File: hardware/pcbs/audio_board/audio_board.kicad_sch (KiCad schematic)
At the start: 26 parts, among them J2 I2C, J3 AudioJack3, J9 SPI, U4 MCP1700x-330xxMB, U5 AP7313-18SAG-7

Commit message: audio_board, power_board: update shop and part links
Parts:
- C5, C6: Part (none) -> C 10uF 16V 0805
- J2: Part (none) -> Header_1x04
- J3: Part (none) -> SJ1-3533NG; Shop (none) -> https://eu.mouser.com/ProductDetail/490-SJ1-3533NG
- J9: Part (none) -> Header_1x06
- R11, R12, R13, R14: Part (none) -> R 1kΩ 0603
- U4: Part (none) -> MCP1700T-3302E/MB; Shop (none) -> https://store.comet.bg/Catalogue/Product/6561/
- U4: Part (none) -> 2x Header_1x24
- U5: Part (none) -> AP7313-18SAG-7; Shop (none) -> https://eu.mouser.com/ProductDetail/Diodes-Incorporated/AP7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
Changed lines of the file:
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@@
 			)
 		)
+		(property "Part" "R 1kΩ 0603"
+			(at 34.29 25.4 0)
+			(effects
+				(font
+					(size 1.27 1.27)
+				)
+				(hide yes)
+			)
+		)
 		(pin "1"
 		)
@@
 			)
 		)
+		(property "Part" "C 10uF 16V 0805"
+			(at 52.07 180.34 0)
+			(effects
+				(font
+					(size 1.27 1.27)
+				)
+				(hide yes)
+			)
+		)
 		(pin "1"
 		)
@@
 			)
 		)
+		(property "Part" "R 1kΩ 0603"
+			(at 26.67 25.4 0)
+			(effects
+				(font
+					(size 1.27 1.27)
+				)
+				(hide yes)
+			)
+		)
 		(pin "1"
 		)
@@
 			)
 		)
+		(property "Part" "C 10uF 16V 0805"
+			(at 69.85 180.34 0)
+			(effects
+				(font
+					(size 1.27 1.27)
+				)
+				(hide yes)
+			)
+		)
 		(pin "1"
 		)
@@
 			)
 		)
+		(property "Part" "R 1kΩ 0603"
+			(at 48.26 25.4 0)
+			(effects
+				(font
+					(size 1.27 1.27)
+				)
+				(hide yes)
+			)
+		)
 		(pin "1"
 		)
@@
 			)
 		)
+		(property "Part" " SJ1-3533NG "
+			(at 132.08 116.84 0)
+			(effects
+				(font
+					(size 1.27 1.27)
+				)
+				(hide yes)
+			)
+		)
+		(property "Shop" "https://eu.mouser.com/ProductDetail/490-SJ1-3533NG"
+			(at 132.08 116.84 0)
+			(effects
+				(font
+					(size 1.27 1.27)
+				)
+				(hide yes)
+			)
+		)
 		(pin "R"
 		)
@@
 			)
 		)
+		(property "Part" "MCP1700T-3302E/MB"
+			(at 39.37 175.26 0)
+			(effects
+				(font
+					(size 1.27 1.27)
+				)
+				(hide yes)
+			)
+		)
+		(property "Shop" "https://store.comet.bg/Catalogue/Product/6561/"
+			(at 39.37 175.26 0)
+			(effects
+				(font
+					(size 1.27 1.27)
+				)
+				(hide yes)
+			)
+		)
 		(pin "1"
 		)
@@
 			)
 		)
+		(property "Part" "Header_1x04"
+			(at 73.66 133.35 0)
+			(effects
+				(font
+					(size 1.27 1.27)
+				)
+				(hide yes)
+			)
+		)
 		(pin "1"
 		)
@@
 			)
 		)
+		(property "Part" "R 1kΩ 0603"
+			(at 40.64 25.4 0)
+			(effects
+				(font
+					(size 1.27 1.27)
+				)
+				(hide yes)
+			)
+		)
 		(pin "1"
 		)
@@
 			)
 		)
+		(property "Part" "C 10uF 16V 0805"
+			(at 95.25 180.34 0)
+			(effects
+				(font
+					(size 1.27 1.27)
+				)
+				(hide yes)
+			)
+		)
 		(pin "1"
 		)
@@
 			)
 		)
+		(property "Part" "C 10uF 16V 0805"
+			(at 118.11 180.34 0)
+			(effects
+				(font
+					(size 1.27 1.27)
+				)
+				(hide yes)
+			)
+		)
 		(pin "1"
 		)
@@
 			)
 		)
+		(property "Part" "AP7313-18SAG-7 "
+			(at 130.81 171.45 0)
+			(effects
+				(font
+					(size 1.27 1.27)
+				)
+				(hide yes)
+			)
+		)
+		(property "Shop" "https://eu.mouser.com/ProductDetail/Diodes-Incorporated/AP7313-18SAG-7?qs=vIZ3oKQCLxpD8%252Bvczs1wyQ%3D%3D"
+			(at 130.81 171.45 0)
+			(effects
+				(font
+					(size 1.27 1.27)
+				)
+				(hide yes)
+			)
+		)
 		(pin "1"
 		)
@@
 			)
 		)
+		(property "Part" "2x Header_1x24"
+			(at 38.1 48.26 0)
+			(effects
+				(font
+					(size 1.27 1.27)
+				)
+				(hide yes)
+			)
+		)
 		(pin "0"
 		)
@@
 			)
 		)
+		(property "Part" "C 10uF 16V 0805"
+			(at 26.67 180.34 0)
+			(effects
+				(font
+					(size 1.27 1.27)
+				)
+				(hide yes)
+			)
+		)
 		(pin "1"
 		)
@@
 			)
 		)
+		(property "Part" "Header_1x06"
+			(at 81.28 107.95 0)
+			(effects
+				(font
+					(size 1.27 1.27)
+				)
+				(hide yes)
+			)
+		)
 		(pin "1"
 		)
@@
 			)
 		)
+		(property "Part" "C 10uF 16V 0805"
+			(at 146.05 180.34 0)
+			(effects
+				(font
+					(size 1.27 1.27)
+				)
+				(hide yes)
+			)
+		)
 		(pin "1"
 		)
@@
 			(at 82.55 175.26 0)
 			(effects
+				(font
+					(size 1.27 1.27)
+				)
+				(hide yes)
+			)
+		)
+		(property "Part" "MCP1700T-3302E/MB"
+			(at 82.55 175.26 0)
+			(effects
+				(font
+					(size 1.27 1.27)
+				)
+				(hide yes)
+			)
+		)
+		(property "Shop" "https://store.comet.bg/Catalogue/Product/6561/"
+			(at 82.55 175.26 0)
+			(effects

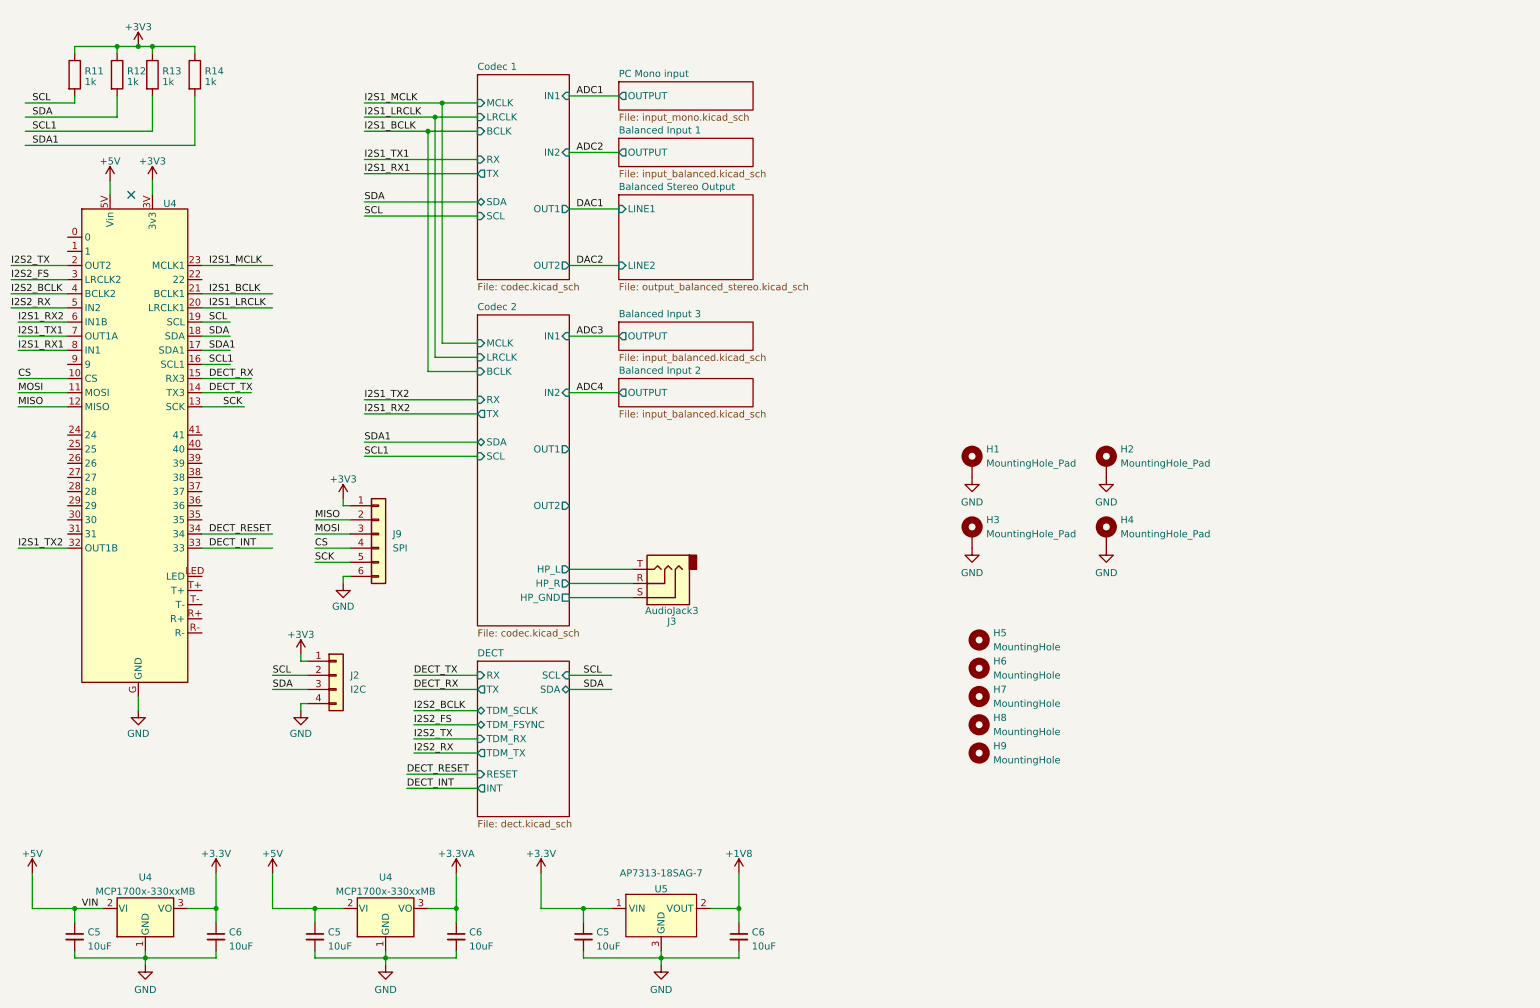
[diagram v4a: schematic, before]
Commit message: Audio board revision C
* Switched the neutrik jacks to NC3FAH2 instead of FAH1 so the jacks
  with an extra ground pin fit (but the FAH1 ones also still fit)
* Added traces for optional leds (marked DNP)
* Fixed up the opamp orientation for the XLR outputs
* Moved the LCD connector to the other side of the board and switched to
  an MTA-100 connector
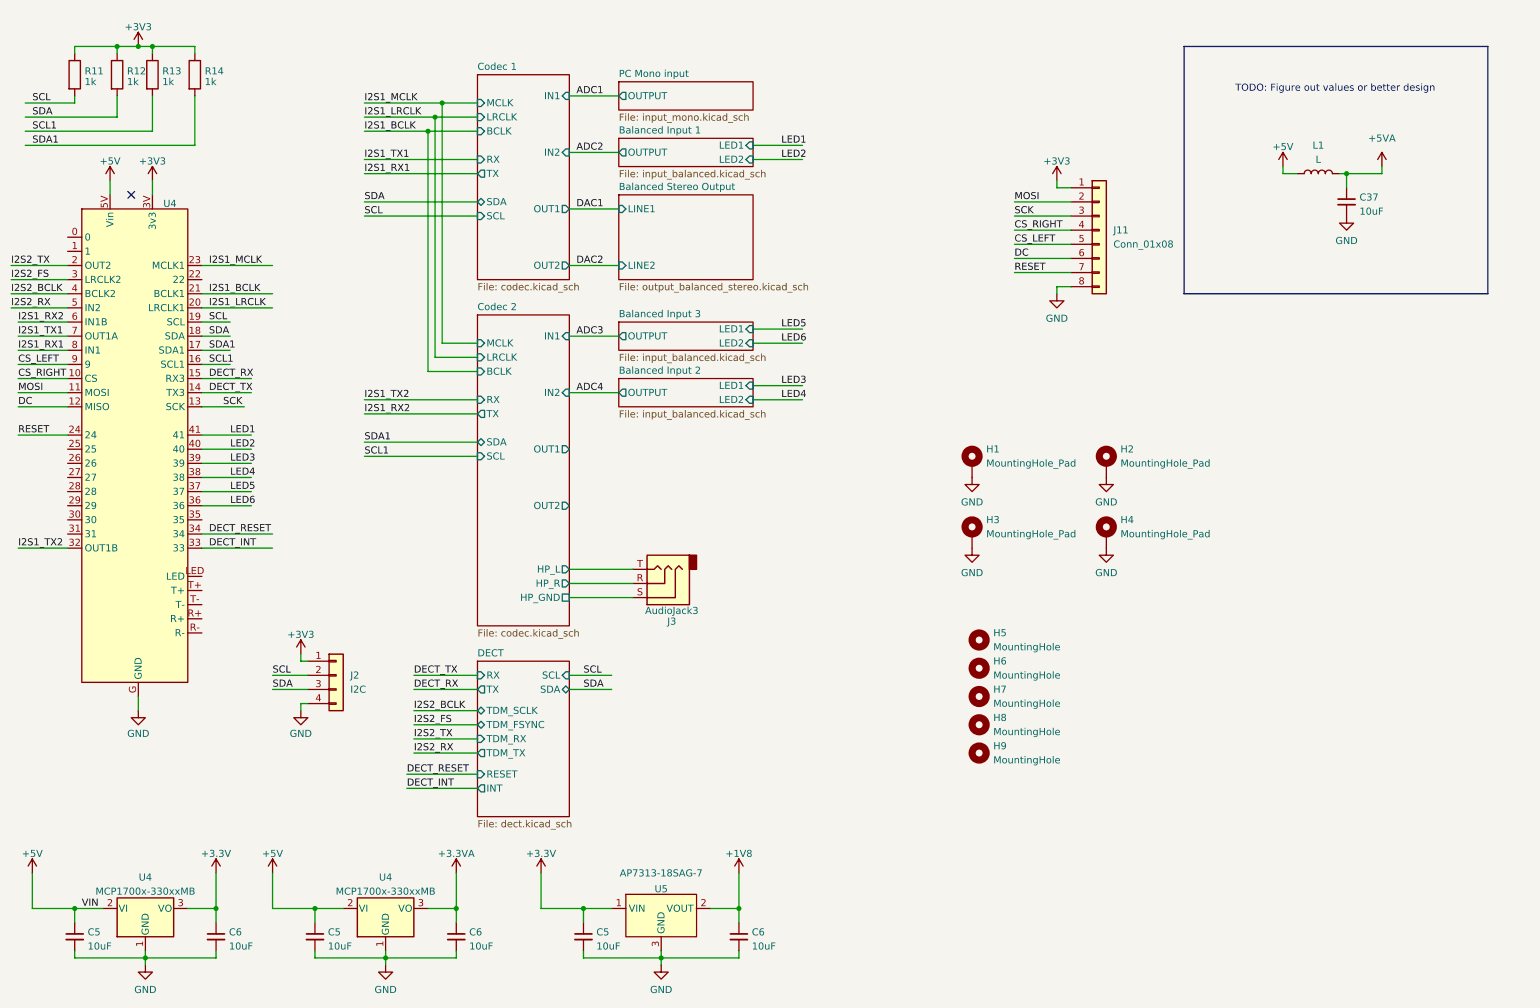
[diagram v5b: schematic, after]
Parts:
- removed J9: SPI, Connector_PinHeader_2.54mm:PinHeader_1x06_P2.54mm_Vertical, symbol Connector_Generic:Conn_01x06
- added C37: 10uF, Capacitor_SMD:C_0805_2012Metric_Pad1.18x1.45mm_HandSolder, symbol Device:C_Small
- added J11: Conn_01x08, Library:mta100_01x8_P2.54_647050-8, symbol Connector_Generic:Conn_01x08
- added L1: L, Inductor_SMD:L_0805_2012Metric, symbol Device:L
- C5, C6: Part C 10uF 16V 0805 -> (none)
- J2: Part Header_1x04 -> (none)
- J3: Part SJ1-3533NG -> (none); Shop https://eu.mouser.com/ProductDetail/490-SJ1-3533NG -> (none)
- R11, R12, R13, R14: Part R 1kΩ 0603 -> (none)
- U4: Part MCP1700T-3302E/MB -> (none); Shop https://store.comet.bg/Catalogue/Product/6561/ -> (none)
- U4: Part 2x Header_1x24 -> (none)
- U5: Part AP7313-18SAG-7 -> (none); Shop https://eu.mouser.com/ProductDetail/Diodes-Incorporated/AP7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 -> (none)
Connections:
- net +3V3: now also J11.1 (Pin_1)
- net +5V: now also L1.1
- net GND: now also C37.2, J11.8 (Pin_8)
- net MOSI: now also J11.2 (Pin_2)
- net SCK: now also J11.3 (Pin_3)
- net RESET: now reaches U4.24
- net RESET: now also J11.7 (Pin_7)
- net LED6: now reaches U4.36
- net LED5: now reaches U4.37
- net LED4: now reaches U4.38
- net LED3: now reaches U4.39
- net LED2: now reaches U4.40
- net LED1: now reaches U4.41
- net CS_LEFT: now reaches U4.9
- net CS_LEFT: now also J11.5 (Pin_5)
- net CS renamed CS_RIGHT
- net CS_RIGHT: now also J11.4 (Pin_4)
- net MISO renamed DC
- net DC: now also J11.6 (Pin_6)
- new net +5VA: C37.1, L1.2
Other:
- sheet Balanced Input 1 ports: added LED1, LED2; removed none
- sheet Balanced Input 2 ports: added LED1, LED2; removed none
- sheet Balanced Input 3 ports: added LED1, LED2; removed none
- note added: "TODO: Figure out values or better design"

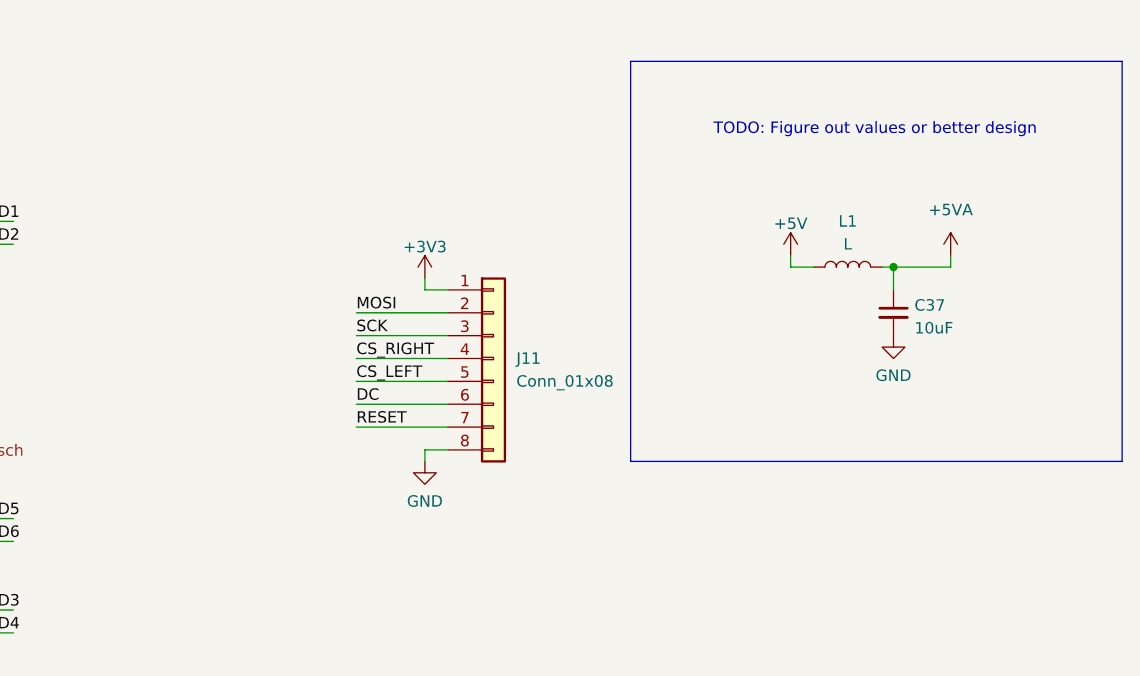
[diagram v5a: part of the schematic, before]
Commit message: Audio board Rev. C fixes
* Switch opamp to OPA1678
* Fix filter resistor on inputs from 22 ohm to 220 ohm
* Make the board 4 layers for a better ground plane
* Implement an RC filter for the opamp 5V line
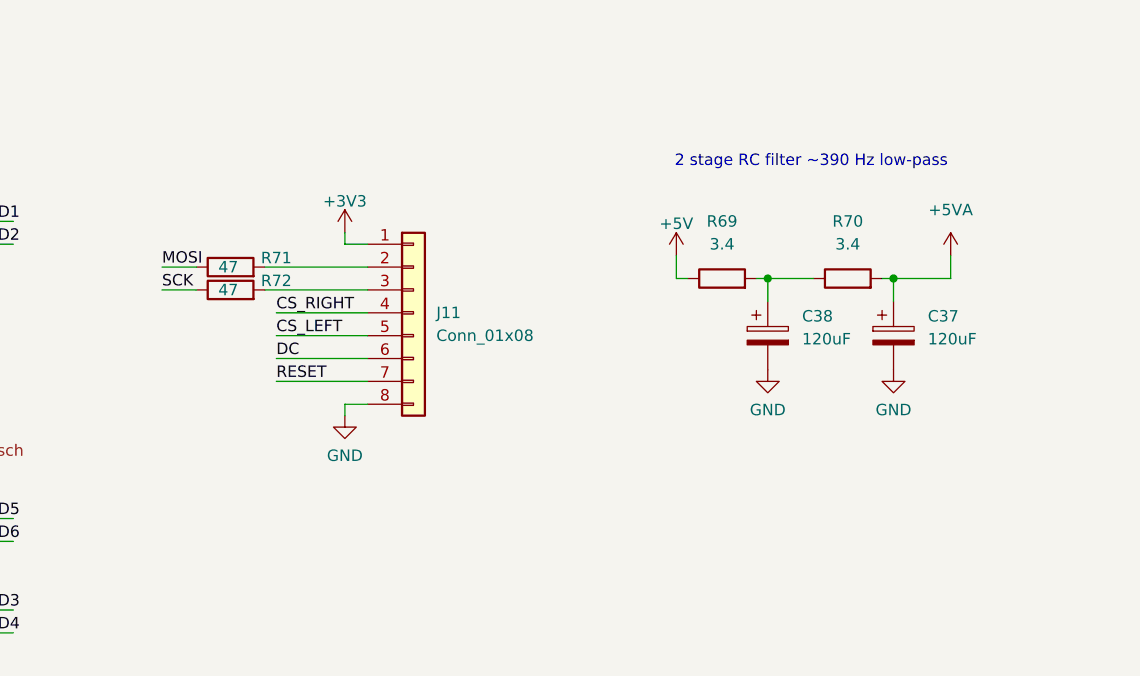
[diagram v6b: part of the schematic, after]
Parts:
- removed C37: 10uF, Capacitor_SMD:C_0805_2012Metric_Pad1.18x1.45mm_HandSolder, symbol Device:C_Small
- removed L1: L, Inductor_SMD:L_0805_2012Metric, symbol Device:L
- added C37, C38: 120uF, Capacitor_THT:CP_Radial_D5.0mm_P2.00mm, symbol Device:C_Polarized
- added R69, R70: 3.4, Resistor_SMD:R_0603_1608Metric_Pad0.98x0.95mm_HandSolder, symbol Device:R
- added R71, R72: 47, Resistor_SMD:R_0603_1608Metric, symbol Device:R
- C5, C6: MPN (none) -> 885012107014
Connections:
- net +5V: now also R69.1
- net +5VA: now also C37.1, R70.2
- net GND: now also C37.2, C38.2
- net MOSI: now also R71.1; no longer J11.2 (Pin_2)
- net SCK: now also R72.1; no longer J11.3 (Pin_3)
- new net: J11.2 (Pin_2), R71.2
- new net: J11.3 (Pin_3), R72.2
- new net: C38.1, R69.2, R70.1
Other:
- note added: "2 stage RC filter ~390 Hz low-pass"
- note removed: "TODO: Figure out values or better design"
- moved on the sheet: J11

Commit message: pcbs: update purchase info
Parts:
- C37, C38: Part (none) -> CP 120μF 16V P2; Shop (none) -> https://store.comet.bg/Catalogue/Product/29518/
- C5, C6: Part (none) -> C 10μF 16V 0805; Shop (none) -> https://store.comet.bg/Catalogue/Product/36934/
- J11: MPN (none) -> 640456-8; Part (none) -> 640456-8; Shop (none) -> https://eu.mouser.com/ProductDetail/TE-Connectivity-AMP/640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
- J2: Part (none) -> Header_1x04
- J3: Part (none) -> SJ1-3533NG; Shop (none) -> https://eu.mouser.com/ProductDetail/490-SJ1-3533NG
- R11, R12, R13, R14: Part (none) -> R 1kΩ 125mW 1% 0603; Shop (none) -> https://store.comet.bg/Catalogue/Product/3458/
- R69, R70: Part (none) -> R 3.4Ω 125mW 1% 0603; Shop (none) -> https://eu.mouser.com/ProductDetail/YAGEO/RC0603FR-073R4L?q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
- R71, R72: Part (none) -> R 47Ω 125mW 1% 0603; Shop (none) -> https://store.comet.bg/Catalogue/Product/4392/
- U4: Part (none) -> MCP1700T-3302E/MB; Shop (none) -> https://store.comet.bg/Catalogue/Product/6561/
- U4: Part (none) -> 2x Header_1x24, Teensy 4.1
- U5: Part (none) -> AP7313-18SAG-7; Shop (none) -> https://eu.mouser.com/ProductDetail/Diodes-Incorporated/AP7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

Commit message: boards: update boms again
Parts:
- C37, C38: Part CP 120μF 16V P2 -> CP 220μF 16V P2
- U4: Part 2x Header_1x24, Teensy 4.1 -> 2x HeaderSocket_1x24, Teensy 4.1
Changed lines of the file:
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@@
 			)
 		)
-		(property "Part" "CP 120μF 16V P2"
+		(property "Part" "CP 220μF 16V P2"
 			(at 241.3 50.8 0)
 			(effects
@@
 			)
 		)
-		(property "Part" "2x Header_1x24, Teensy 4.1"
+		(property "Part" "2x HeaderSocket_1x24, Teensy 4.1"
 			(at 38.1 48.26 0)
 			(effects
@@
 			)
 		)
-		(property "Part" "CP 120μF 16V P2"
+		(property "Part" "CP 220μF 16V P2"
 			(at 255.27 50.8 0)
 			(effects
